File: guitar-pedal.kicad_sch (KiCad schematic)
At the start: 48 parts, among them J1 USB_OTG, J2 AudioJack2, J3 AudioJack2, J4 Barrel_Jack, SW1 SW_SPDT, SW2 SW_3PDT, SW3 SW_Push_SPDT, SW4 SW_Push_SPDT, U1 Opamp_Dual, U2 AZ1117-3.3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

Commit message: replace GNDREF with GND; and Reset and Boot switches; prepare to change 9V->3.3V LDO with 5V->3.3V
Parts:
- removed U2: AZ1117-3.3, symbol Regulator_Linear:AZ1117-3.3
- added C?: 0.1uF, symbol Device:C_Small
- added SW?: Reset, symbol Switch:SW_Push
- added SW?: Boot, symbol Switch:SW_Push
- R1: value 1MF -> 1M
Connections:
- net +5V: now also C9.1
- net +9V: no longer C9.1
- net at C8.1, R8.2, U3.3 (EN): now also SW?.1
- net at U3.27 (GPIO0): now also C?.2, SW?.2
- net GNDREF renamed GND
- net GND: now also C?.1, SW?.1, SW?.2
- no-connect marks 27 -> 26
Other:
- note added: "Boot Pin"

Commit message: add test points
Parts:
- added J?: Test_Headers, symbol Connector:Conn_01x10_Male
- SW1: value SW_SPDT -> Power
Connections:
- net +3V3: now also J?.8 (Pin_8)
- net +5V: now also J?.6 (Pin_6)
- net +9V: now also J?.1 (Pin_1)
- net BIASED_IN: now also J?.2 (Pin_2)
- net BIASED_OUT: now also J?.3 (Pin_3)
- net GND: now also J?.10 (Pin_10)
- net RAW_IN: now also J?.4 (Pin_4)
- net RAW_OUT: now also J?.5 (Pin_5)
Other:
- note added: "Test Point Header Pins"
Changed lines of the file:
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@@
+    (stroke (width 0) (type default) (color 0 0 0 0))
+  )
+  (wire (pts (xy 358.648 97.282) (xy 370.332 97.282))
     (stroke (width 0) (type default) (color 0 0 0 0))
   )
@@
     (stroke (width 0) (type default) (color 0 0 0 0))
   )
+  (wire (pts (xy 357.632 104.902) (xy 370.332 104.902))
+    (stroke (width 0) (type default) (color 0 0 0 0))
+  )
   (wire (pts (xy 102.87 41.91) (xy 100.33 41.91))
     (stroke (width 0) (type default) (color 0 0 0 0))
@@
     (stroke (width 0) (type default) (color 0 0 0 0))
   )
+  (wire (pts (xy 358.14 109.982) (xy 370.332 109.982))
+    (stroke (width 0) (type default) (color 0 0 0 0))
+  )
   (wire (pts (xy 367.03 46.99) (xy 351.79 46.99))
     (stroke (width 0) (type default) (color 0 0 0 0))
@@
     (stroke (width 0) (type default) (color 0 0 0 0))
   )
+  (wire (pts (xy 357.632 87.122) (xy 370.332 87.122))
+    (stroke (width 0) (type default) (color 0 0 0 0))
+  )
   (polyline (pts (xy 22.86 113.03) (xy 69.85 113.03))
     (stroke (width 0) (type default) (color 0 0 0 0))
@@
     (stroke (width 0) (type default) (color 0 0 0 0))
   )
+  (wire (pts (xy 358.648 89.662) (xy 370.332 89.662))
+    (stroke (width 0) (type default) (color 0 0 0 0))
+  )
   (polyline (pts (xy 129.54 153.67) (xy 129.54 182.88))
     (stroke (width 0) (type default) (color 0 0 0 0))
@@
     (stroke (width 0) (type default) (color 0 0 0 0))
   )
+  (wire (pts (xy 357.632 99.822) (xy 370.332 99.822))
+    (stroke (width 0) (type default) (color 0 0 0 0))
+  )
   (wire (pts (xy 168.91 142.24) (xy 168.91 129.54))
     (stroke (width 0) (type default) (color 0 0 0 0))
@@
     (stroke (width 0) (type default) (color 0 0 0 0))
   )
+  (wire (pts (xy 358.648 92.202) (xy 370.332 92.202))
+    (stroke (width 0) (type default) (color 0 0 0 0))
+  )
   (wire (pts (xy 59.69 163.83) (xy 59.69 166.37))
     (stroke (width 0) (type default) (color 0 0 0 0))
@@
   )
   (polyline (pts (xy 154.686 81.28) (xy 206.248 81.026))
+    (stroke (width 0) (type default) (color 0 0 0 0))
+  )
+  (wire (pts (xy 358.648 94.742) (xy 370.332 94.742))
     (stroke (width 0) (type default) (color 0 0 0 0))
   )
@@
     (effects (font (size 1.27 1.27)) (justify left bottom))
   )
+  (text "Test Point Header Pins" (at 369.316 81.28 0)
+    (effects (font (size 1.27 1.27)) (justify left bottom))
+  )
   (text "9V DC Supply" (at 22.86 69.85 0)
     (effects (font (size 1.27 1.27)) (justify left bottom))
@@
     (effects (font (size 1.27 1.27)) (justify right bottom))
   )
+  (label "RAW_OUT" (at 358.648 97.282 0)
+    (effects (font (size 1.27 1.27)) (justify left bottom))
+  )
+  (label "BIASED_OUT" (at 358.648 92.202 0)
+    (effects (font (size 1.27 1.27)) (justify left bottom))
+  )
   (label "SWITCHED_OUT" (at 351.79 41.91 0)
     (effects (font (size 1.27 1.27)) (justify left bottom))
@@
     (effects (font (size 1.27 1.27)) (justify right bottom))
   )
+  (label "BIASED_IN" (at 358.648 89.662 0)
+    (effects (font (size 1.27 1.27)) (justify left bottom))
+  )
   (label "D-" (at 45.72 43.18 180)
     (effects (font (size 1.27 1.27)) (justify right bottom))
+  )
+  (label "RAW_IN" (at 358.648 94.742 0)
+    (effects (font (size 1.27 1.27)) (justify left bottom))
   )
   (label "D+" (at 185.42 173.99 0)
@@
     (pin "2")
   )
+  (symbol (lib_id "power:+5V") (at 357.632 99.822 0) (unit 1)
+    (in_bom yes) (on_board yes)
+    (property "Reference" "#PWR?" (id 0) (at 357.632 103.632 0)
+      (effects (font (size 1.27 1.27)) hide)
+    )
+    (property "Value" "+5V" (id 1) (at 360.426 98.806 0))
+    (property "Footprint" "" (id 2) (at 357.632 99.822 0)
+      (effects (font (size 1.27 1.27)) hide)
+    )
+    (property "Datasheet" "" (id 3) (at 357.632 99.822 0)
+      (effects (font (size 1.27 1.27)) hide)
+    )
+    (pin "1")
+  )
   (symbol (lib_id "power:GND") (at 298.45 134.62 0) (unit 1)
     (in_bom yes) (on_board yes) (fields_autoplaced)
@@
     (in_bom yes) (on_board yes) (fields_autoplaced)
     (property "Reference" "SW1" (id 0) (at 55.88 76.2 0))
-    (property "Value" "SW_SPDT" (id 1) (at 55.88 78.74 0))
+    (property "Value" "Power" (id 1) (at 55.88 78.74 0))
     (property "Footprint" "" (id 2) (at 55.88 83.82 0)
       (effects (font (size 1.27 1.27)) hide)
@@
     (pin "1")
   )
+  (symbol (lib_id "power:+9V") (at 357.632 87.122 0) (unit 1)
+    (in_bom yes) (on_board yes)
+    (property "Reference" "#PWR?" (id 0) (at 357.632 90.932 0)
+      (effects (font (size 1.27 1.27)) hide)
+    )
+    (property "Value" "+9V" (id 1) (at 360.426 85.852 0))
+    (property "Footprint" "" (id 2) (at 357.632 87.122 0)
+      (effects (font (size 1.27 1.27)) hide)
+    )
+    (property "Datasheet" "" (id 3) (at 357.632 87.122 0)
+      (effects (font (size 1.27 1.27)) hide)
+    )
+    (pin "1")
+  )
   (symbol (lib_id "power:PWR_FLAG") (at 44.45 83.82 0) (unit 1)
     (in_bom yes) (on_board yes)
@@
     (pin "1")
   )
+  (symbol (lib_id "power:+3V3") (at 357.632 104.902 0) (unit 1)
+    (in_bom yes) (on_board yes)
+    (property "Reference" "#PWR?" (id 0) (at 357.632 108.712 0)
+      (effects (font (size 1.27 1.27)) hide)
+    )
+    (property "Value" "+3V3" (id 1) (at 360.934 103.886 0))
+    (property "Footprint" "" (id 2) (at 357.632 104.902 0)
+      (effects (font (size 1.27 1.27)) hide)
+    )
+    (property "Datasheet" "" (id 3) (at 357.632 104.902 0)
+      (effects (font (size 1.27 1.27)) hide)
+    )
+    (pin "1")
+  )
   (symbol (lib_id "power:GND") (at 90.17 50.8 0) (unit 1)
     (in_bom yes) (on_board yes) (fields_autoplaced)
@@
     (pin "2")
     (pin "3")
+  )
+  (symbol (lib_id "Connector:Conn_01x10_Male") (at 375.412 97.282 0) (mirror y) (unit 1)
+    (in_bom yes) (on_board yes) (fields_autoplaced)
+    (property "Reference" "J?" (id 0) (at 377.19 97.2819 0)
+      (effects (font (size 1.27 1.27)) (justify right))
+    )
+    (property "Value" "Test_Headers" (id 1) (at 377.19 99.8219 0)
+      (effects (font (size 1.27 1.27)) (justify right))
+    )
+    (property "Footprint" "" (id 2) (at 375.412 97.282 0)
+      (effects (font (size 1.27 1.27)) hide)
+    )
+    (property "Datasheet" "~" (id 3) (at 375.412 97.282 0)
+      (effects (font (size 1.27 1.27)) hide)
+    )
+    (pin "1")
+    (pin "10")
+    (pin "2")
+    (pin "3")
+    (pin "4")
+    (pin "5")
+    (pin "6")
+    (pin "7")
+    (pin "8")
+    (pin "9")
   )
   (symbol (lib_id "Device:C_Small") (at 170.18 93.98 0) (mirror y) (unit 1)
@@
     (pin "2")
     (pin "3")
+  )
+  (symbol (lib_id "power:GND") (at 358.14 109.982 0) (unit 1)
+    (in_bom yes) (on_board yes)
+    (property "Reference" "#PWR?" (id 0) (at 358.14 116.332 0)
+      (effects (font (size 1.27 1.27)) hide)
+    )
+    (property "Value" "GND" (id 1) (at 361.442 111.506 0))
+    (property "Footprint" "" (id 2) (at 358.14 109.982 0)
+      (effects (font (size 1.27 1.27)) hide)
+    )
+    (property "Datasheet" "" (id 3) (at 358.14 109.982 0)
+      (effects (font (size 1.27 1.27)) hide)
+    )
+    (pin "1")
   )
   (symbol (lib_id "power:GND") (at 105.41 142.24 0) (unit 1)
@@
       (reference "#PWR0137") (unit 1) (value "+3V3") (footprint "")
     )
+    (path "/062a0745-38e6-4708-ba01-afbe8ef4ca89"
+      (reference "#PWR?") (unit 1) (value "+5V") (footprint "")
+    )
     (path "/0800cfc1-bd54-4130-b8f3-8e5d17421165"
       (reference "#PWR?") (unit 1) (value "GND") (footprint "")
@@
       (reference "#PWR?") (unit 1) (value "GND") (footprint "")
     )
+    (path "/71168ea5-b05e-4dab-9a51-ccbd3bea5f63"
+      (reference "#PWR?") (unit 1) (value "+9V") (footprint "")
+    )
     (path "/76ab871d-2213-4827-9ef6-e2fdccee6cc0"
       (reference "#PWR?") (unit 1) (value "GND") (footprint "")
@@
       (reference "#PWR?") (unit 1) (value "GND") (footprint "")
     )
+    (path "/7fcbd881-6412-4837-8346-4a7ef67c8942"
+      (reference "#PWR?") (unit 1) (value "+3V3") (footprint "")
+    )
     (path "/7fed61af-eaa2-45a5-89ba-7d0cc8a80ac0"
       (reference "#PWR?") (unit 1) (value "GND") (footprint "")
@@
     )
     (path "/b2e84e90-d1c8-40f7-94c5-e154afc105ed"
+      (reference "#PWR?") (unit 1) (value "GND") (footprint "")
+    )
+    (path "/b7c34765-c854-4906-a9d5-1ec8768bcd7c"
       (reference "#PWR?") (unit 1) (value "GND") (footprint "")
     )
@@
       (reference "J4") (unit 1) (value "Barrel_Jack") (footprint "")
     )
+    (path "/8b87fcfc-4d33-4e63-b56b-68b24da21f98"
+      (reference "J?") (unit 1) (value "Test_Headers") (footprint "")
+    )
     (path "/d150c883-e641-4548-a17d-a4c8e8775a90"
       (reference "POT1") (unit 1) (value "B10K") (footprint "")
@@
     )
     (path "/282e0857-44f2-4d34-8b60-2c5f3acb829b"
-      (reference "SW1") (unit 1) (value "SW_SPDT") (footprint "")
+      (reference "SW1") (unit 1) (value "Power") (footprint "")
     )
     (path "/6da2e811-c5e0-40c6-9fcd-4ef2253b5fc9"

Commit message: remove 9V supply and fix value suffixes
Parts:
- removed C11, C12: 10uF, symbol Device:C_Small
- removed J4: Barrel_Jack, symbol Connector:Barrel_Jack
- removed SW1: Power, symbol Switch:SW_SPDT
- removed U4: AP7375, symbol Regulator_Linear:AP7375
- added C?: 0.1uF, symbol Device:C_Small
- added C?: 10uF, symbol Device:C_Small
- added PCM3002E?: PCM3002E, symbol lib-guitar-pedal:PCM3002E
- C2: value 1u -> 1uF
- R5: value 1MF -> 1M
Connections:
- new net: C?.1, C?.1, PCM3002E?.14 (VDD)
- no-connect marks 26 -> 25
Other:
- note added: "Boot Button"
- note removed: "5V Supply for input & output processing sections (not sure if those are needed)"
- note removed: "9V DC Supply"
- note removed: "Boot Pin"
- moved on the sheet: C10, C9

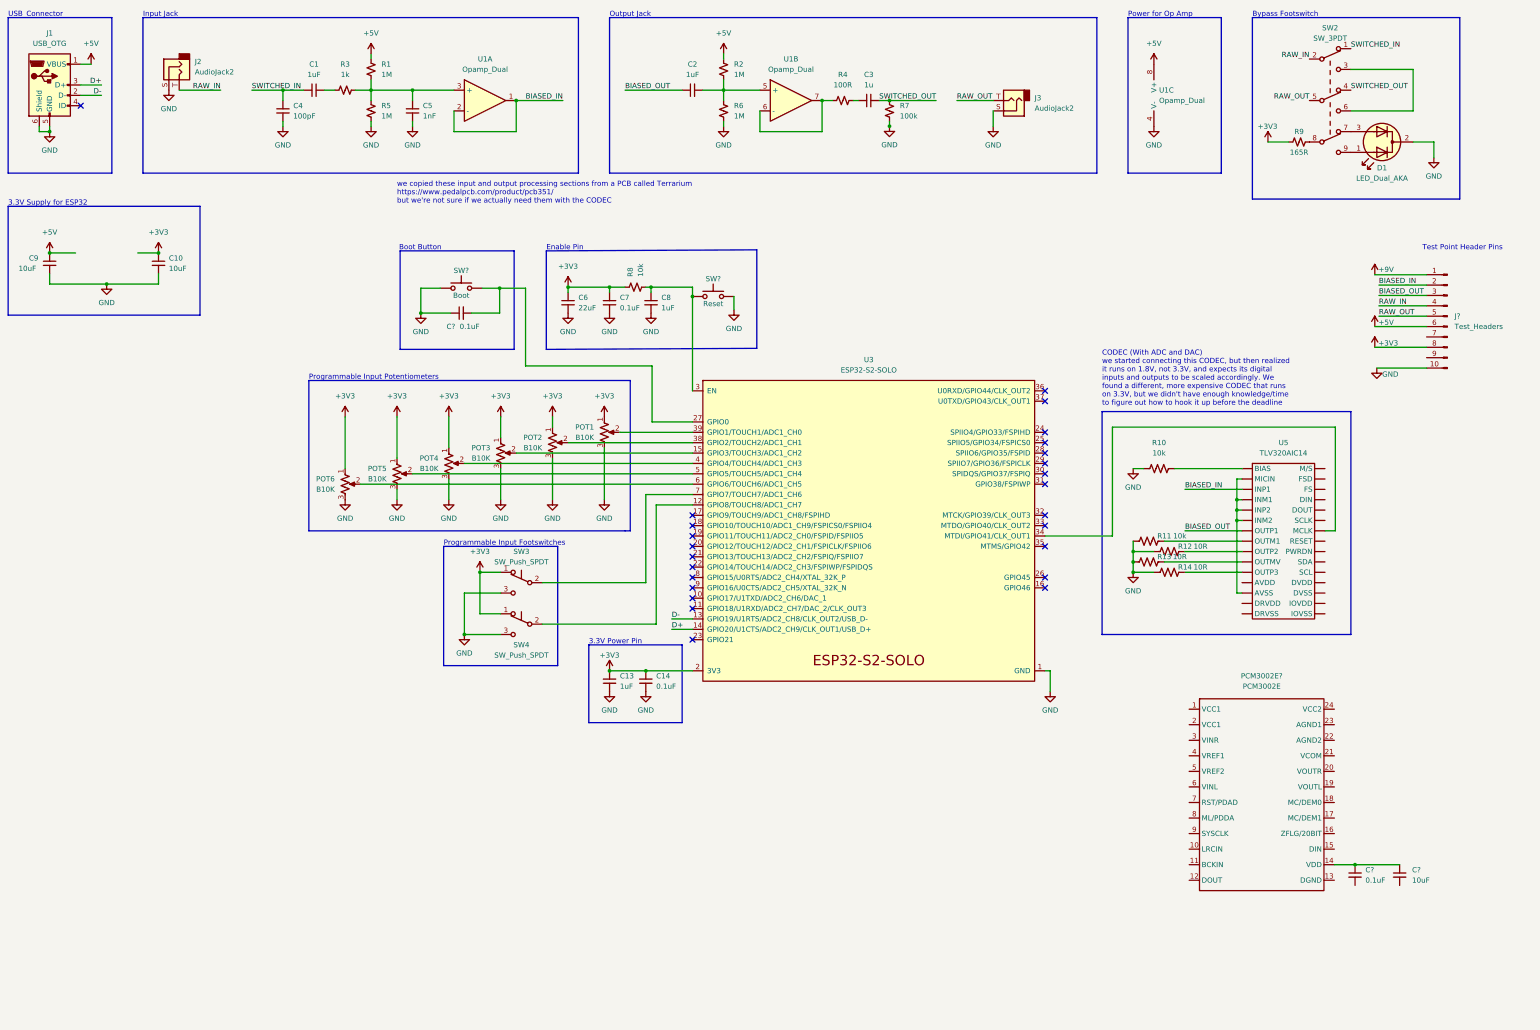
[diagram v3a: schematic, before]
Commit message: pre-design review tweaks
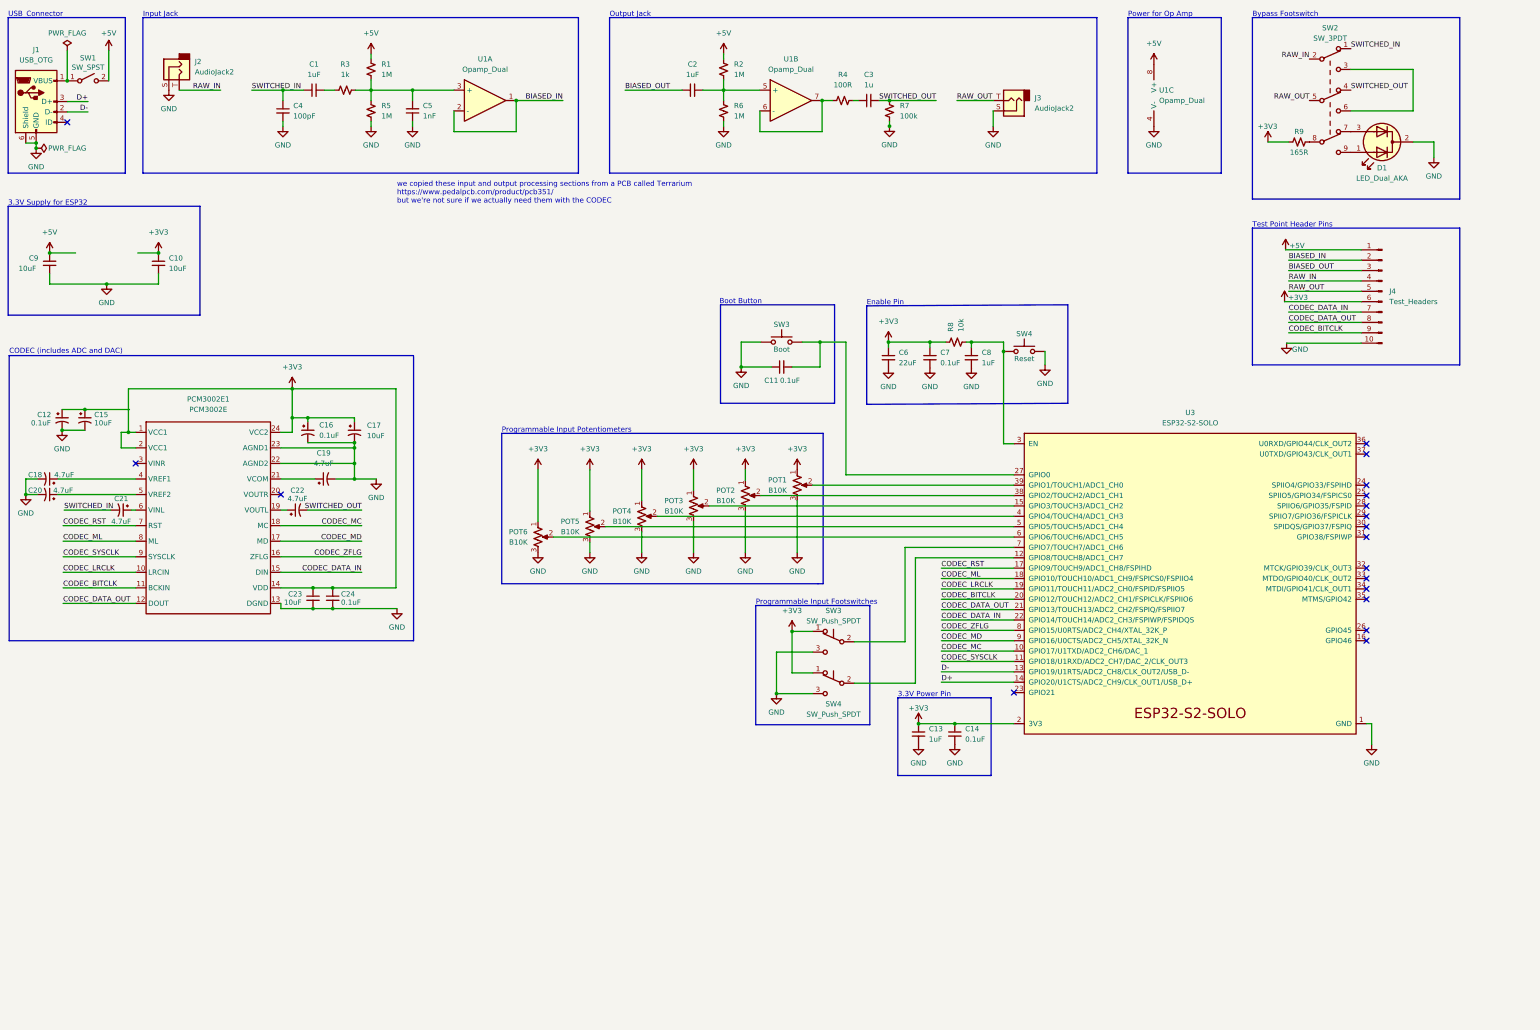
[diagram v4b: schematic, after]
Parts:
- removed R10, R11: 10k, symbol Device:R_US
- removed R12, R13, R14: 10R, symbol Device:R_US
- removed U5: TLV320AIC14, symbol Audio:TLV320AIC14
- added C12, C16: 0.1uF, symbol Device:C_Polarized_Small_US
- added C15, C17: 10uF, symbol Device:C_Polarized_Small_US
- added C18, C19, C20, C21, C22: 4.7uF, symbol Device:C_Polarized_Small_US
- added SW1: SW_SPST, symbol Switch:SW_SPST
- gave numbers to parts that had none: 7
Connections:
- net +9V is gone; now on net +5V: J4.1 (Pin_1)
- net +3V3: now also C23.1, C24.1, J4.6 (Pin_6), PCM3002E1.1 (VCC1), PCM3002E1.14 (VDD), PCM3002E1.2 (VCC1), PCM3002E1.24 (VCC2), C16.1, C17.1; no longer J4.8 (Pin_8)
- net +5V: now also SW1.2 (B); no longer J1.1 (VBUS), J4.6 (Pin_6)
- net GND: now also C23.2, C24.2, PCM3002E1.13 (DGND), PCM3002E1.22 (AGND2), PCM3002E1.23 (AGND1), C12.2, C15.2, C16.2, C17.2, C18.2, C19.2, C20.2
- net SWITCHED_IN: now also C21.2
- net SWITCHED_OUT: now also C22.2
- net CODEC_LRCLK: now reaches PCM3002E1.10 (LRCIN)
- net CODEC_LRCLK: now also U3.19 (GPIO11/TOUCH11/ADC2_CH0/FSPID/FSPIIO5)
- net CODEC_BITCLK: now reaches PCM3002E1.11 (BCKIN)
- net CODEC_BITCLK: now also J4.9 (Pin_9), U3.20 (GPIO12/TOUCH12/ADC2_CH1/FSPICLK/FSPIIO6)
- net CODEC_DATA_OUT: now reaches PCM3002E1.12 (DOUT)
- net CODEC_DATA_OUT: now also J4.8 (Pin_8), U3.21 (GPIO13/TOUCH13/ADC2_CH2/FSPIQ/FSPIIO7)
- net CODEC_DATA_IN: now reaches PCM3002E1.15 (DIN)
- net CODEC_DATA_IN: now also J4.7 (Pin_7), U3.22 (GPIO14/TOUCH14/ADC2_CH3/FSPIWP/FSPIDQS)
- net CODEC_ZFLG: now reaches PCM3002E1.16 (ZFLG)
- net CODEC_ZFLG: now also U3.8 (GPIO15/U0RTS/ADC2_CH4/XTAL_32K_P)
- net CODEC_MD: now reaches PCM3002E1.17 (MD)
- net CODEC_MD: now also U3.9 (GPIO16/U0CTS/ADC2_CH5/XTAL_32K_N)
- net CODEC_MC: now reaches PCM3002E1.18 (MC)
- net CODEC_MC: now also U3.10 (GPIO17/U1TXD/ADC2_CH6/DAC_1)
- net at PCM3002E1.19 (VOUTL): now also C22.1
- net at PCM3002E1.21 (VCOM): now also C19.1
- net at PCM3002E1.4 (VREF1): now also C18.1
- net at PCM3002E1.5 (VREF2): now also C20.1
- net at PCM3002E1.6 (VINL): now also C21.1
- net CODEC_RST: now reaches PCM3002E1.7 (RST)
- net CODEC_RST: now also U3.17 (GPIO9/TOUCH9/ADC1_CH8/FSPIHD)
- net CODEC_ML: now reaches PCM3002E1.8 (ML)
- net CODEC_ML: now also U3.18 (GPIO10/TOUCH10/ADC1_CH9/FSPICS0/FSPIIO4)
- net CODEC_SYSCLK: now reaches PCM3002E1.9 (SYSCLK)
- net CODEC_SYSCLK: now also U3.11 (GPIO18/U1RXD/ADC2_CH7/DAC_2/CLK_OUT3)
- new net: J1.1 (VBUS), SW1.1 (A)
- new net: C12.1, C15.1
- no-connect marks 25 -> 18
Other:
- note added: "CODEC (includes ADC and DAC)"
- note removed: "CODEC (With ADC and DAC) we started connecting this CODEC, but then realized it runs on 1.8V, not 3.3V, and expects its digital inputs and outputs to be scaled accordingly. We found a different, more expensive CODEC that runs on 3.3V, but we didn't have enough knowledge/time to figure out how to hook it up before the deadline"
- moved on the sheet: C11, C13, C14, C23, C24, C6, C7, C8, J1, J4, PCM3002E1, POT1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
